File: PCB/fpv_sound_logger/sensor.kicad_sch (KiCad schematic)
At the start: 8 parts, among them U2 INMP441ACEZ-R7

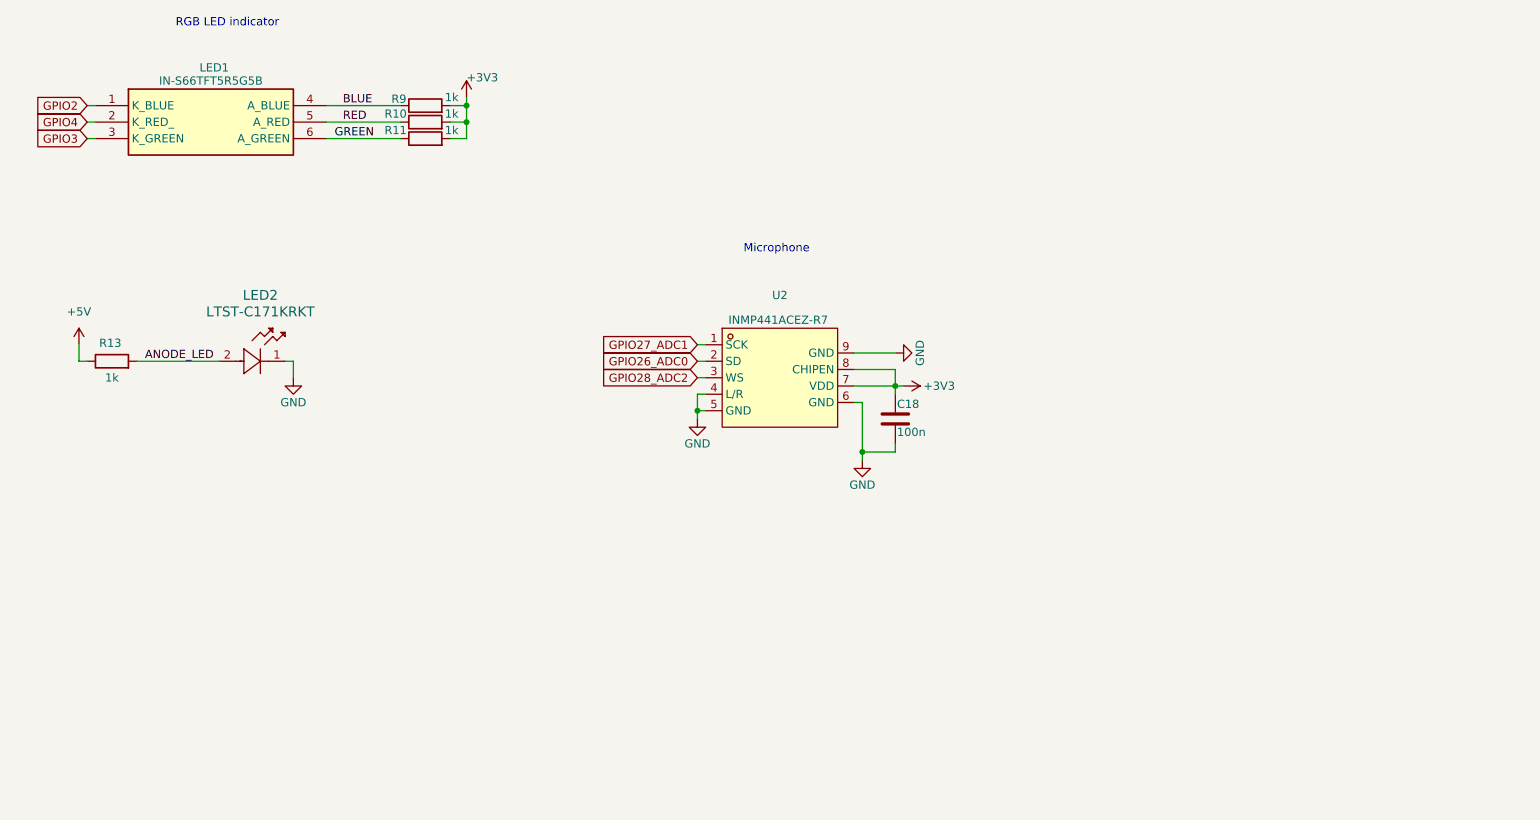
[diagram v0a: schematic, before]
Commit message: place new components and started routing for v2
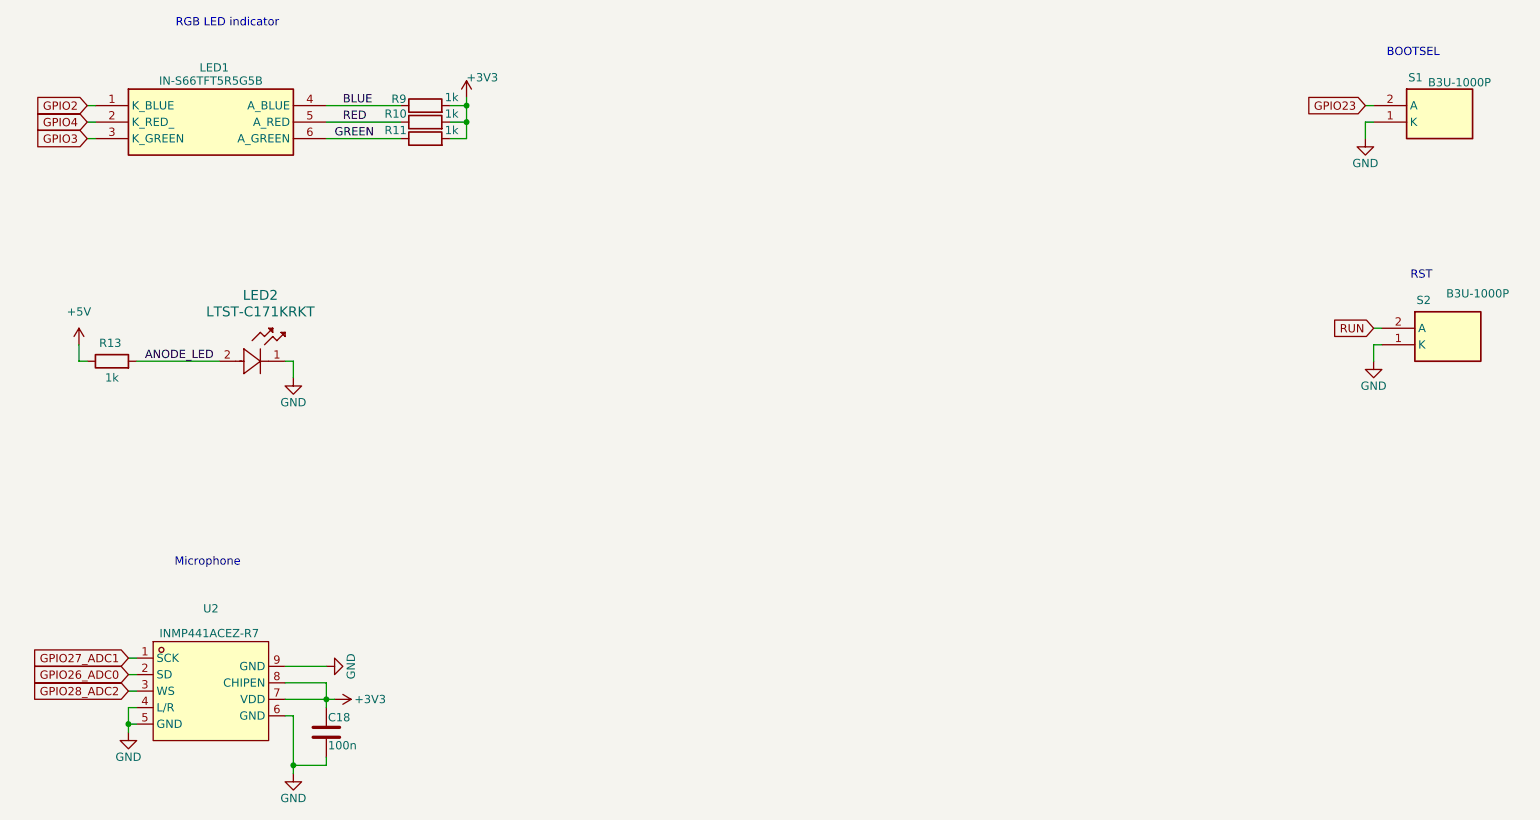
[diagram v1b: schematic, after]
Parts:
- added S1, S2: B3U-1000P, fpv_sound_logger:B3U-1000P, symbol SoundLogger:B3U-1000P
- LED1: Manufacturer Inolux -> (none)
- R10, R11, R13, R9: footprint Capacitor_SMD:C_0805_2012Metric -> Resistor_SMD:R_0805_2012Metric
- U2: Manufacturer TDK InvenSense -> (none)
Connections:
- net GND: now also S1.1 (K), S2.1 (K)
- new net GPIO23: S1.2 (A)
- new net RUN: S2.2 (A)
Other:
- note added: "BOOTSEL"
- note added: "RST"
- moved on the sheet: C18, U2

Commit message: Update component footprints and add manufacturer details in sensor schematic
- Changed resistor footprint from R_0805 to R_0603 for multiple components.
- Updated manufacturer part numbers, manufacturers, suppliers, and supplier parts for various components.
- Added manufacturer and supplier information for OMRON components.
- Removed outdated datasheet link and replaced with relevant part numbers for clarity.
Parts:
- C18: footprint Capacitor_SMD:C_0805_2012Metric -> Capacitor_SMD:C_0603_1608Metric; MANUFACTURER (none) -> Samsung Electro-Mechanics; Manufacturer_Part_Number (none) -> CL10B104KB8NNNC; Supplier (none) -> LCSC; Supplier Part (none) -> C1591
- LED2: MANUFACTURER (none) -> LITEON; Manufacturer_Part_Number (none) -> LTST-C171KRKT; Supplier (none) -> LCSC; Supplier Part (none) -> C284871
- R10, R11, R13, R9: footprint Resistor_SMD:R_0805_2012Metric -> Resistor_SMD:R_0603_1608Metric; MANUFACTURER (none) -> PANASONIC; Manufacturer_Part_Number (none) -> ERJ3EKF1001V; Supplier (none) -> LCSC; Supplier Part (none) -> C118155
- S1, S2: MANUFACTURER (none) -> OMRON; Supplier (none) -> LCSC; Supplier Part (none) -> C231329
- U2: Manufacturer_Part_Number INMP441ACEZ-R7 -> (none); Supplier LCSC -> (none); Supplier Part C22379536 -> (none)

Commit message: Refactor code structure for improved readability and maintainability
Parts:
- removed C18: 100n, Capacitor_SMD:C_0603_1608Metric, symbol Device:C
- removed U2: INMP441ACEZ-R7, fpv_sound_logger:MID-SMD_L4.7-W3.8_INMP441ACEZ, symbol SoundLogger:INMP441ACEZ-R7
- added C19: 1u, Capacitor_SMD:C_0603_1608Metric, symbol Device:C
- added MIC1: (no value), fpv_sound_logger:MIC-TH_BD6.0-P1.90-D0.4-L-FD_GMI6050P-2CXXDB, symbol SoundLogger:GMI6050P-36DB
- added R14: 2k2, Resistor_SMD:R_0603_1608Metric, symbol Device:R
- LED1: MANUFACTURER (none) -> EVERLIGHT; Manufacturer_Part_Number IN-S66TFT5R5G5B -> 19-337/R6GHBHC-A01/2T; Supplier (none) -> LCSC; Supplier Part (none) -> C264519
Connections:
- net +5V: now also R14.2
- net GND: now also MIC1.1 (+)
- net GPIO26_ADC0: now also C19.2
- new net: C19.1, MIC1.2 (-), R14.1

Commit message: Update PCB design and netlist for fpv_sound_logger
- Added new segments and vias for microphone and GPIO connections in the PCB layout.
- Removed redundant segments related to GPIO26_ADC0 and MIC1 in the PCB layout.
- Updated active layer in the project file to improve visibility.
- Modified visible layers in the project file for better layer management.
- Adjusted netlist to include new connections for MIC1 and GPIO26_ADC0.
- Changed manufacturer and supplier part numbers for components in the schematic.
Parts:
- C19: Manufacturer_Part_Number CL10B104KB8NNNC -> CL10B105KA8NNNC; Supplier Part C1591 -> C29936
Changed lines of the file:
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@@
 			)
 		)
-		(property "Manufacturer_Part_Number" "CL10B104KB8NNNC"
+		(property "Manufacturer_Part_Number" "CL10B105KA8NNNC"
 			(at 60.96 127 0)
 			(hide yes)
@@
 			)
 		)
-		(property "Supplier Part" "C1591"
+		(property "Supplier Part" "C29936"
 			(at 60.96 127 0)
 			(hide yes)
